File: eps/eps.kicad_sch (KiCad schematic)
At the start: 0 parts

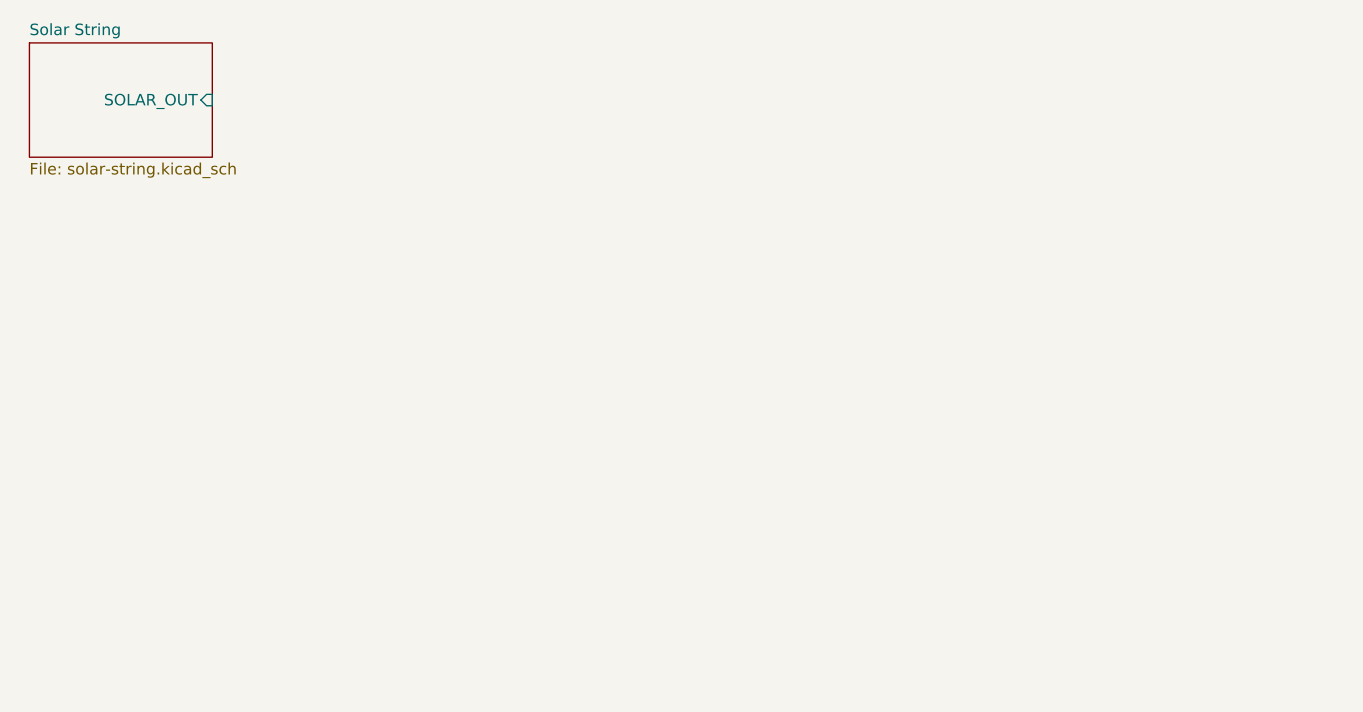
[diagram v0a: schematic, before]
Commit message: add LTC3130 buck-boost MPPT controller and connect solar strings
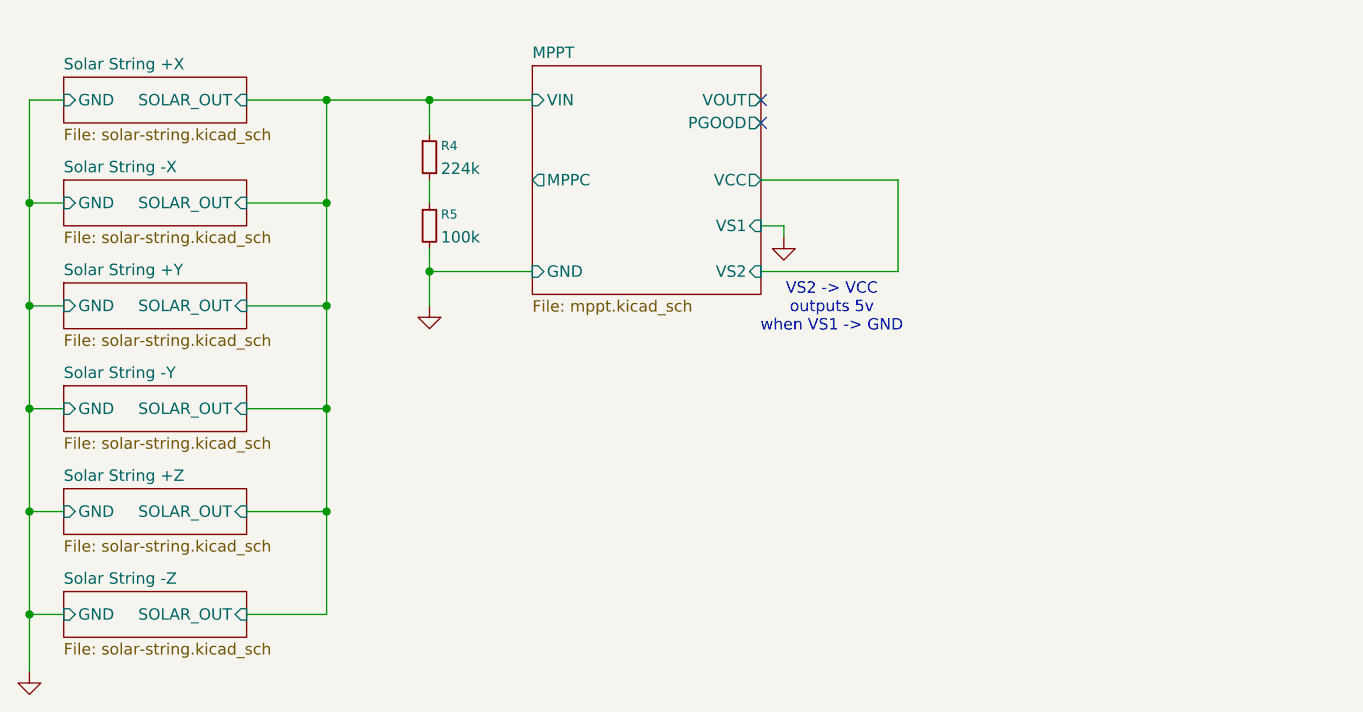
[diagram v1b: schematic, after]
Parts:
- added R4: 224k, symbol Device:R_Small
- added R5: 100k, symbol Device:R_Small
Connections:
- new net: R4.2, R5.1
- new net GND: R5.2
- new net MPPT/VIN: R4.1
- no-connect marks 0 -> 2
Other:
- sheet Solar String renamed Solar String +X
- added sheet MPPT (mppt.kicad_sch)
- added sheet Solar String +Y (solar-string.kicad_sch)
- added sheet Solar String +Z (solar-string.kicad_sch)
- added sheet Solar String -X (solar-string.kicad_sch)
- added sheet Solar String -Y (solar-string.kicad_sch)
- added sheet Solar String -Z (solar-string.kicad_sch)
- sheet Solar String +X ports: added GND; removed none
- note added: "VS2 -> VCC outputs 5v when VS1 -> GND"

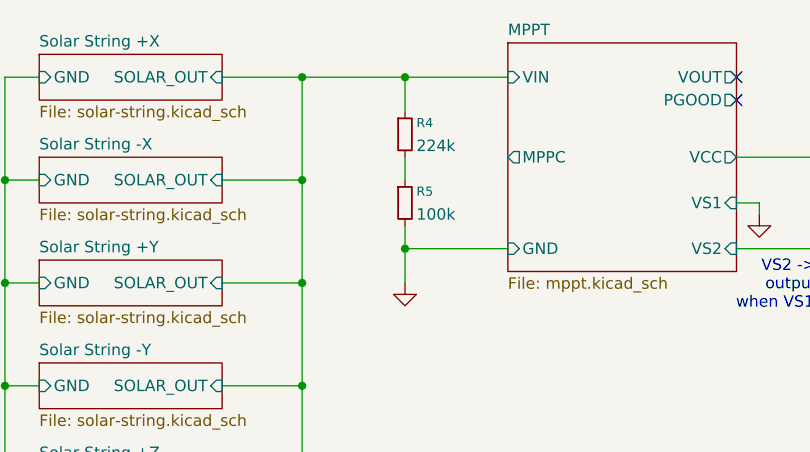
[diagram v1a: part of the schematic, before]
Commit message: eps schematic cleanup + LoRa OBC example
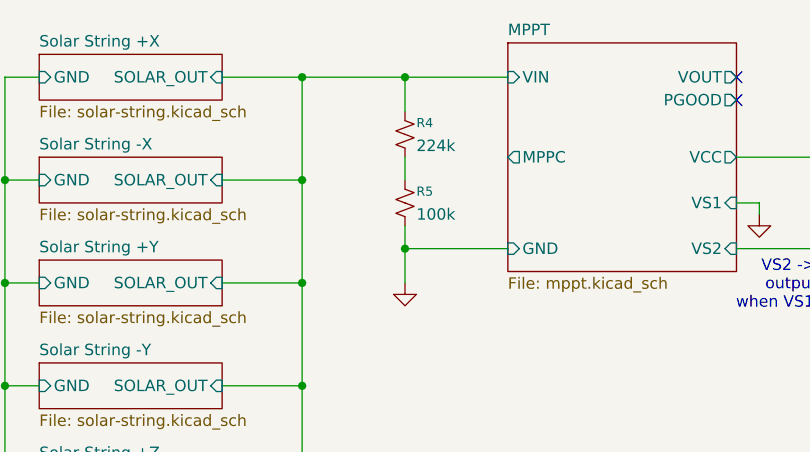
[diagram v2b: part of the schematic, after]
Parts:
- R4, R5: symbol Device:R_Small -> Device:R_Small_US
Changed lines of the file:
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@@
 	)
 	(symbol
-		(lib_id "Device:R_Small")
+		(lib_id "Device:R_Small_US")
 		(at 62.23 29.21 0)
 		(unit 1)
@@
 			)
 		)
-		(property "Description" "Resistor, small symbol"
+		(property "Description" "Resistor, small US symbol"
 			(at 62.23 29.21 0)
 			(effects
@@
 	)
 	(symbol
-		(lib_id "Device:R_Small")
+		(lib_id "Device:R_Small_US")
 		(at 62.23 36.83 0)
 		(unit 1)
@@
 			)
 		)
-		(property "Description" "Resistor, small symbol"
+		(property "Description" "Resistor, small US symbol"
 			(at 62.23 36.83 0)
 			(effects

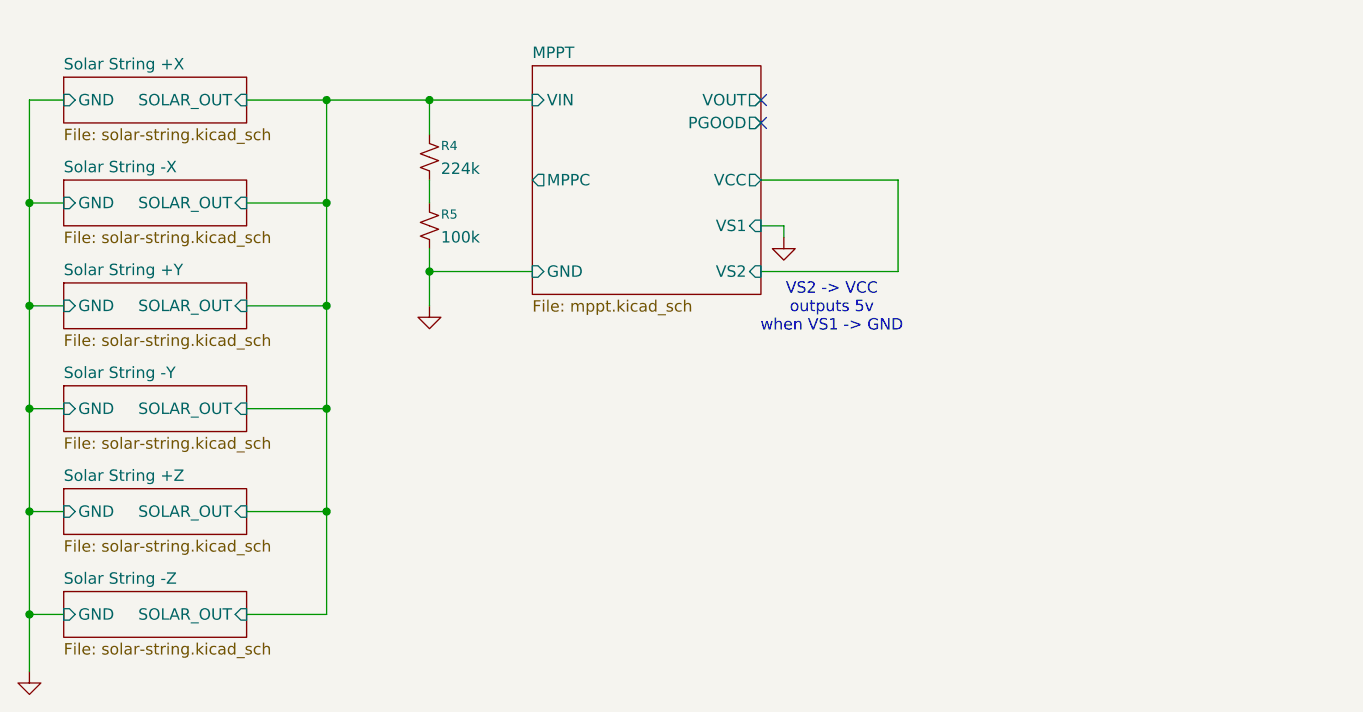
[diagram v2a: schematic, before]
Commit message: add battery charger
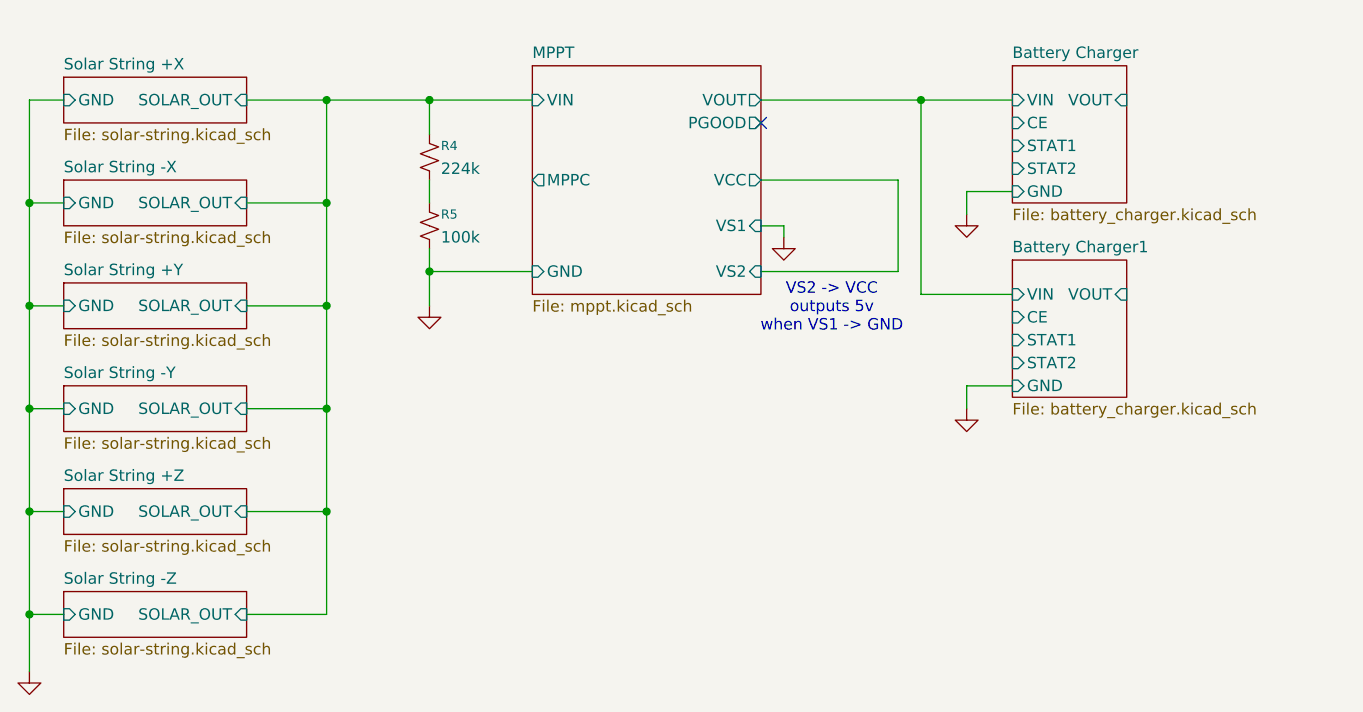
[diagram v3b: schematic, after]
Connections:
- no-connect marks 2 -> 1
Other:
- added sheet Battery Charger (battery_charger.kicad_sch)
- added sheet Battery Charger1 (battery_charger.kicad_sch)
